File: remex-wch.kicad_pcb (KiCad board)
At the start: 4 copper layers, 88.9 x 22.9 mm, 99 parts, among them J1 Conn_01x16, J2 Conn_01x12, J3 USB_C_Receptacle_USB2.0_16P, J4 Micro_SD_Card_Det1, J5 RJ45_Hanrun_HR911130C, J7 JST_PH, SW1 RESET, U1 CH32V307WCU6, U2 RTL8211F, U3 MS5351M, U4 HUSB311, U5 SY6820, U6 LW52xxN11E, U7 LGS5500, U8 PY32F002AW15U, Y1 32.768kHz 12.5 pF Q13FC135000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, Y2 25 MHz 10 pF X322525MOB4SI

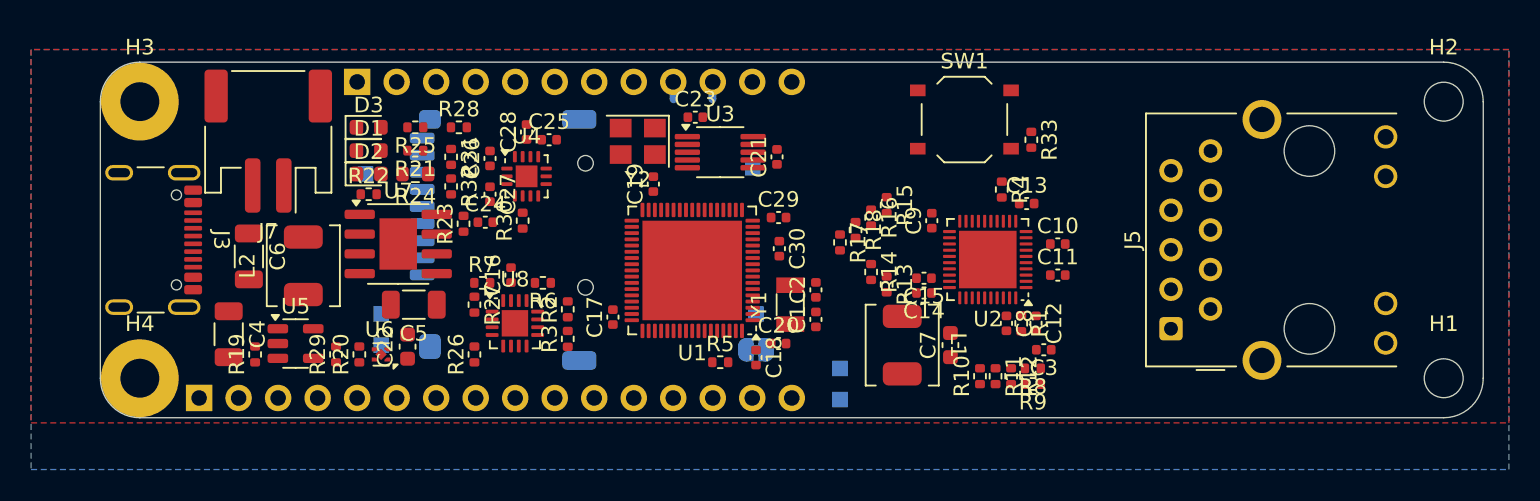
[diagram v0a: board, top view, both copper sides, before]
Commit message: better initial attempt at all the hard signals
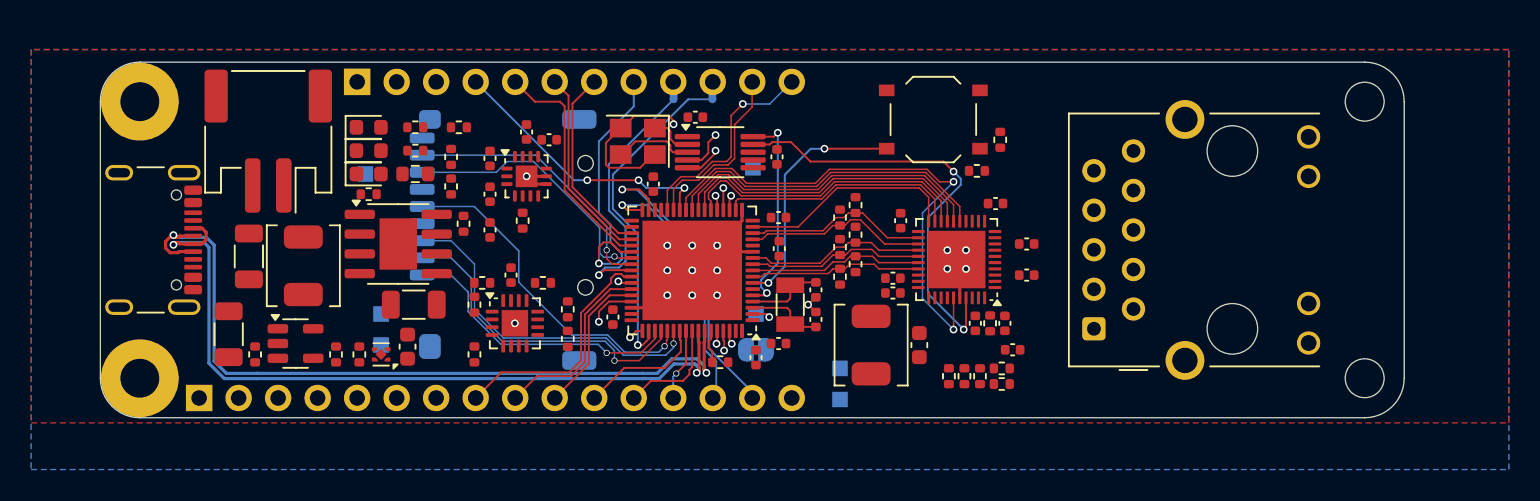
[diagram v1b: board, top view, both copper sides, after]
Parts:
- moved H1 5.08 mm to (125.7, 151.1)
- moved H2 5.08 mm to (125.7, 133.3)
- moved J5 4.95 mm to (110.9, 146.7)
- moved R13 3.04 mm to (92.0, 144.6)
- moved C10 2.00 mm to (104.0, 142.5)
- moved C11 2.00 mm to (104.0, 144.5)
- moved C12 2.00 mm to (102.6, 147.6)
- moved C13 2.00 mm to (102.0, 139.9)
- moved C14 2.00 mm to (95.4, 145.7)
- moved C15 2.00 mm to (95.4, 144.7)
- moved C3 2.00 mm to (103.1, 149.3)
- moved C7 2.00 mm to (97.1, 149.0)
- moved C8 2.00 mm to (100.7, 147.6)
- moved C9 2.00 mm to (95.9, 141.0)
- moved L1 2.00 mm to (94.0, 149.0)
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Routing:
- net /USB_D+: track 0.00 -> 50.4 mm, vias 0 -> 2
- net /USB_D-: track 0.00 -> 49.2 mm, vias 0 -> 2
- net /RGMII_CLK125: track 0.00 -> 33.1 mm, vias 0 -> 2
- net /CLK_ETHPHY: track 0.00 -> 28.0 mm, vias 0 -> 2
- net GND: track 0.00 -> 24.6 mm, vias 0 -> 17
- net /SDIO_CMD: track 0.00 -> 22.2 mm, vias 0 -> 1
- net /SDIO_CLK: track 0.00 -> 21.8 mm, vias 0 -> 1
- net /I2S_WS: track 0.00 -> 21.4 mm, vias 0 -> 1
- net /RGMII_TXD3: track 0.00 -> 21.4 mm
- net /EXT_TX: track 0.00 -> 20.9 mm, vias 0 -> 1
- net /SDIO_D3: track 0.00 -> 20.8 mm, vias 0 -> 1
- net /RGMII_TXD2: track 0.00 -> 20.5 mm
- net /RGMII_TXD1: track 0.00 -> 19.7 mm
- net /RGMII_TXD0: track 0.00 -> 19.0 mm
- net /SDIO_D2: track 0.00 -> 18.7 mm, vias 0 -> 1
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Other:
- board size 88.9 x 22.9 mm -> 83.8 x 22.9 mm

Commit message: work on power section
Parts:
- moved C3 2.06 mm to (105.0, 148.5), turned to -90 degrees
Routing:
- net VBUS: track 0.00 -> 51.0 mm, vias 0 -> 2
- net +5V: track 0.00 -> 36.1 mm, vias 0 -> 3
- net GND: track 24.6 -> 58.3 mm, vias 17 -> 42
- net +BATT: track 0.00 -> 19.6 mm, vias 0 -> 2
- net /EXT_EN: track 0.00 -> 19.2 mm, vias 0 -> 1
- net /ETH_MDI1-: track 0.00 -> 16.5 mm
- net /ETH_MDI3+: track 0.00 -> 10.2 mm
- net /ETH_MDI2-: track 0.00 -> 9.53 mm
- net /ETH_MDI0+: track 0.00 -> 9.53 mm
- net /ETH_MDI1+: track 0.00 -> 9.13 mm
- net /ETH_MDI3-: track 0.00 -> 8.03 mm
- net /ETH_MDI0-: track 0.00 -> 7.40 mm
- net Net-(U7-VSET/LED): track 0.00 -> 6.72 mm
- net /ETH_MDI2+: track 0.00 -> 6.57 mm
- net Net-(U7-NTC): track 0.00 -> 6.04 mm, vias 0 -> 1
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- added copper zone on F.Cu, net +5V
- added copper zone on F.Cu, net +BATT
- added copper zone on F.Cu, net Net-(U7-LX)

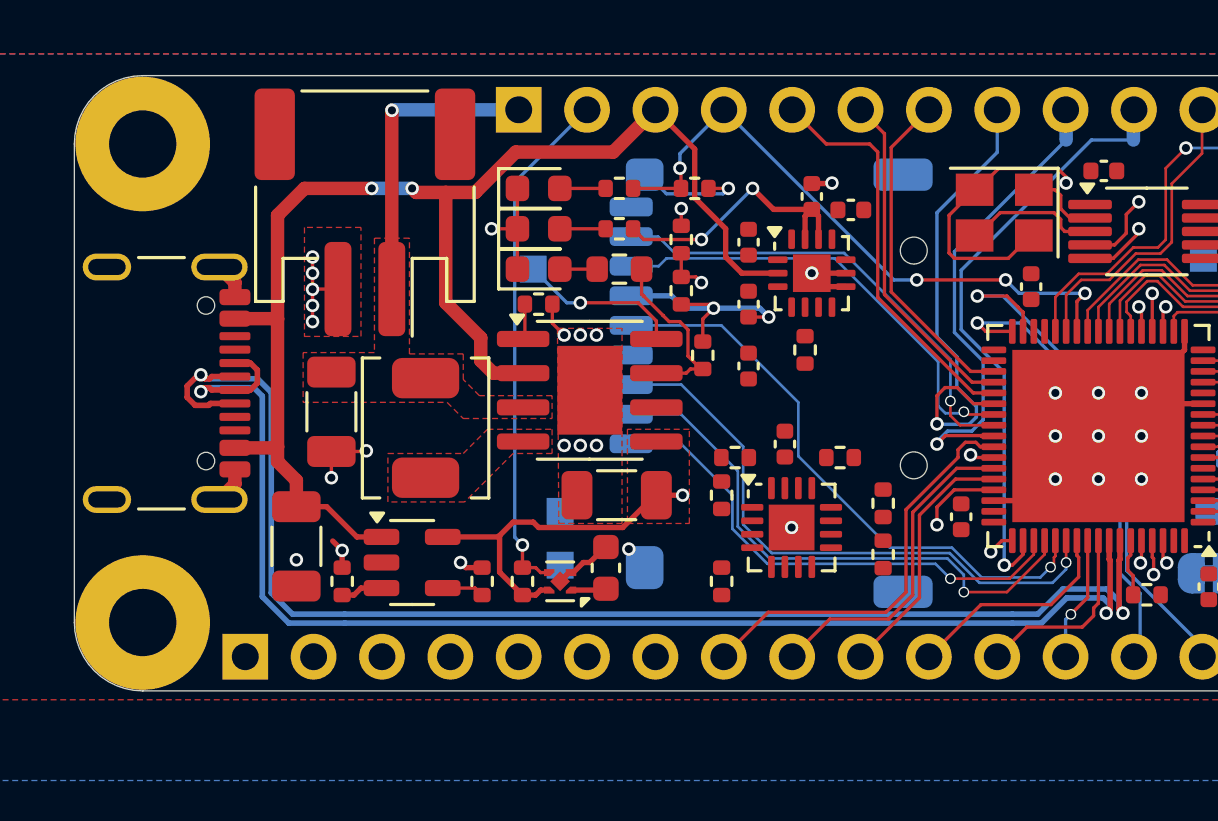
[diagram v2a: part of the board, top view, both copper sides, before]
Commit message: work on usb c mgmt section
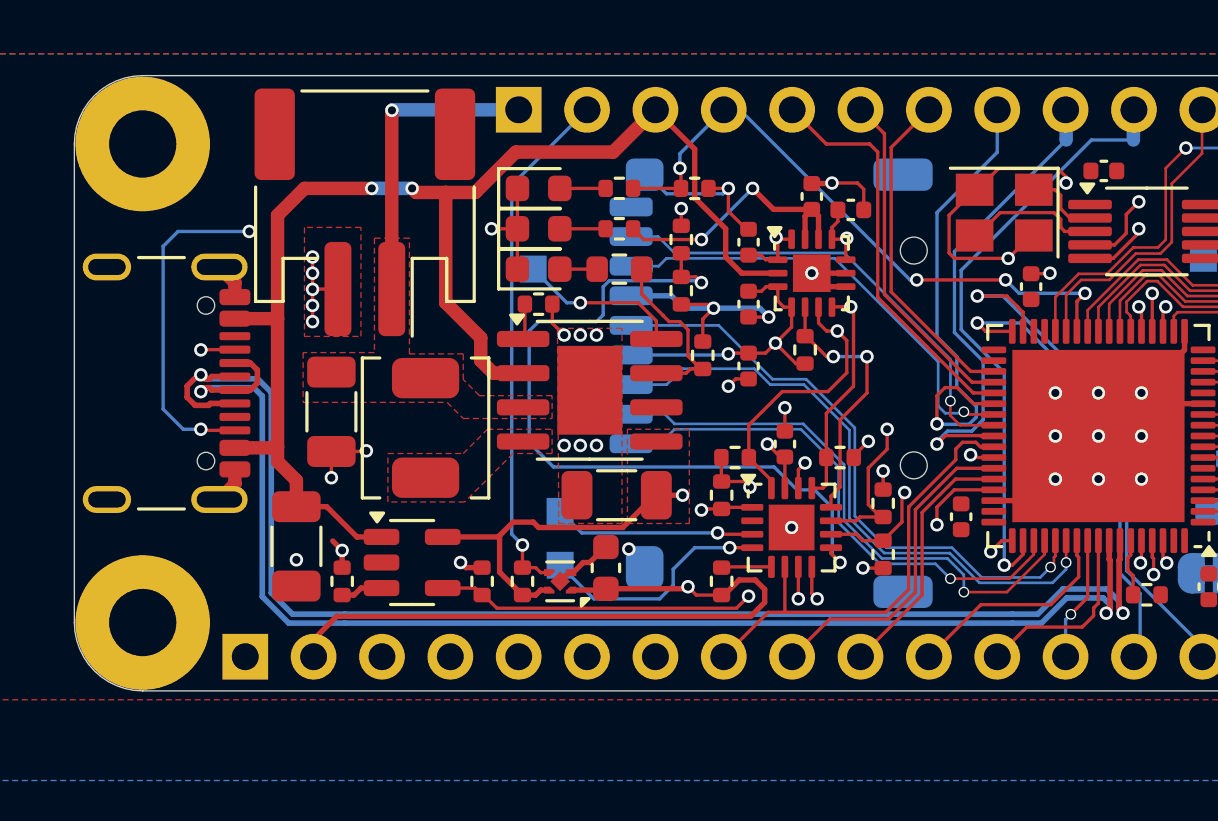
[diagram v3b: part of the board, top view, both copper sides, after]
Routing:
- net +3.3V: track 1.24 -> 62.6 mm, vias 0 -> 7
- net /EXT_A0: track 0.95 -> 37.9 mm
- net /USB_CC2: track 0.00 -> 35.9 mm, vias 0 -> 3
- net /USB_CC1: track 0.00 -> 34.7 mm, vias 0 -> 2
- net /EXT_A1: track 1.41 -> 34.4 mm
- net /EXT_A2: track 0.95 -> 30.5 mm
- net /VBAT_MEAS: track 1.72 -> 28.8 mm, vias 1 -> 2
- net /USB_PW_SW_EN: track 1.57 -> 18.8 mm, vias 0 -> 2
- net /INT_I2C_SCL: track 3.73 -> 14.0 mm, vias 2 -> 3
- net /~{PD_INT}: track 0.00 -> 9.85 mm, vias 0 -> 2
- net /AUX_SWCLK: track 0.00 -> 8.79 mm, vias 0 -> 1
- net /INT_I2C_SDA: track 3.64 -> 12.0 mm, vias 2 -> 3
- net /AUX_SWDIO: track 0.00 -> 7.49 mm, vias 0 -> 1
- net GND: track 58.3 -> 65.4 mm, vias 42 -> 47
- net /~{PHYRST}: track 0.00 -> 5.83 mm, vias 0 -> 1
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
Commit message: work on clock chip
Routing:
- net +3.3V: track 62.6 -> 107.2 mm, vias 7 -> 11
- net /INT_I2C_SCL: track 14.0 -> 44.3 mm
- net /INT_I2C_SDA: track 12.0 -> 39.6 mm
- net /~{RST}: track 15.6 -> 41.2 mm, vias 2 -> 3
- net /~{AUX_INT}: track 2.81 -> 22.7 mm, vias 2 -> 3
- net GND: track 65.4 -> 71.0 mm, vias 47 -> 48
- net /EXT_TX: track 20.9 -> 18.8 mm
- net /EXT_RX: track 18.2 -> 16.5 mm
- net /USB_PW_SW_EN: track 18.8 -> 19.9 mm

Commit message: everything connected
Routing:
- net +3.3V: track 107.2 -> 218.5 mm, vias 11 -> 21
- net /~{RST}: track 41.2 -> 86.1 mm
- net /RGMII_MDIO: track 0.00 -> 31.5 mm, vias 0 -> 2
- net Net-(J5-Pad13): track 0.00 -> 31.2 mm
- net /~{PHYRST}: track 5.83 -> 34.8 mm, vias 1 -> 2
- net /RGMII_MDC: track 0.00 -> 28.3 mm, vias 0 -> 2
- net Net-(U2-DVDD10): track 3.11 -> 30.2 mm, vias 2 -> 5
- net /~{ETH_INT}: track 4.16 -> 30.2 mm, vias 1 -> 2
- net GND: track 71.0 -> 96.8 mm, vias 48 -> 65
- net Net-(J5-Pad11): track 0.00 -> 21.1 mm
- net /EXT_XTRA: track 0.90 -> 19.3 mm, vias 1 -> 2
- net /SWDIO: track 2.89 -> 19.7 mm, vias 1 -> 2
- net /SWCLK: track 0.97 -> 17.2 mm, vias 1 -> 2
- net /ETH_LED_YEL: track 0.00 -> 7.73 mm, vias 0 -> 2
- net /ETH_LED_GRN: track 0.00 -> 6.78 mm
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- added copper zone on F.Cu, net Net-(U2-DVDD10)
- added copper zone on F.Cu, net Net-(U2-REG_OUT)

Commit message: clean up fab layers
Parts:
- JP1: value SolderJumper_2_Bridged -> VBAT

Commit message: correct 10pf crystal
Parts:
- Y2: value 25 MHz 10 pF X322525MOB4SI -> 25 MHz 10 pF X322525MMB4SI
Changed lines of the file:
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@@
 			)
 		)
-		(property "Value" "25 MHz 10 pF X322525MOB4SI"
+		(property "Value" "25 MHz 10 pF X322525MMB4SI"
 			(at 0.3 2 180)
 			(layer "F.Fab")
@@
 			)
 		)
-		(property "LCSC" "C9006"
+		(property "LCSC" "C70582"
 			(at 0 0 180)
 			(unlocked yes)

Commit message: hopefully fix nettie
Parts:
- NT1, NT2: footprint NetTie:NetTie-2_SMD_Pad0.5mm -> parts:nettie_tiny
- moved NT1 0.60 mm to (81.2, 133.3)
- moved NT2 0.60 mm to (83.8, 133.3)
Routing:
- net /EXT_D6: track 0.00 -> 1.11 mm
- net /EXT_D5: track 0.00 -> 1.10 mm
